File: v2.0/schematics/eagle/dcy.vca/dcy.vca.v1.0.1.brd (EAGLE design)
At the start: 100 x 50 mm, 104 parts, among them IC1 LM324N, IC2 4001N, IC3 TL074P, IC4 4001N, IC5 LM324N, IC6 TL074P

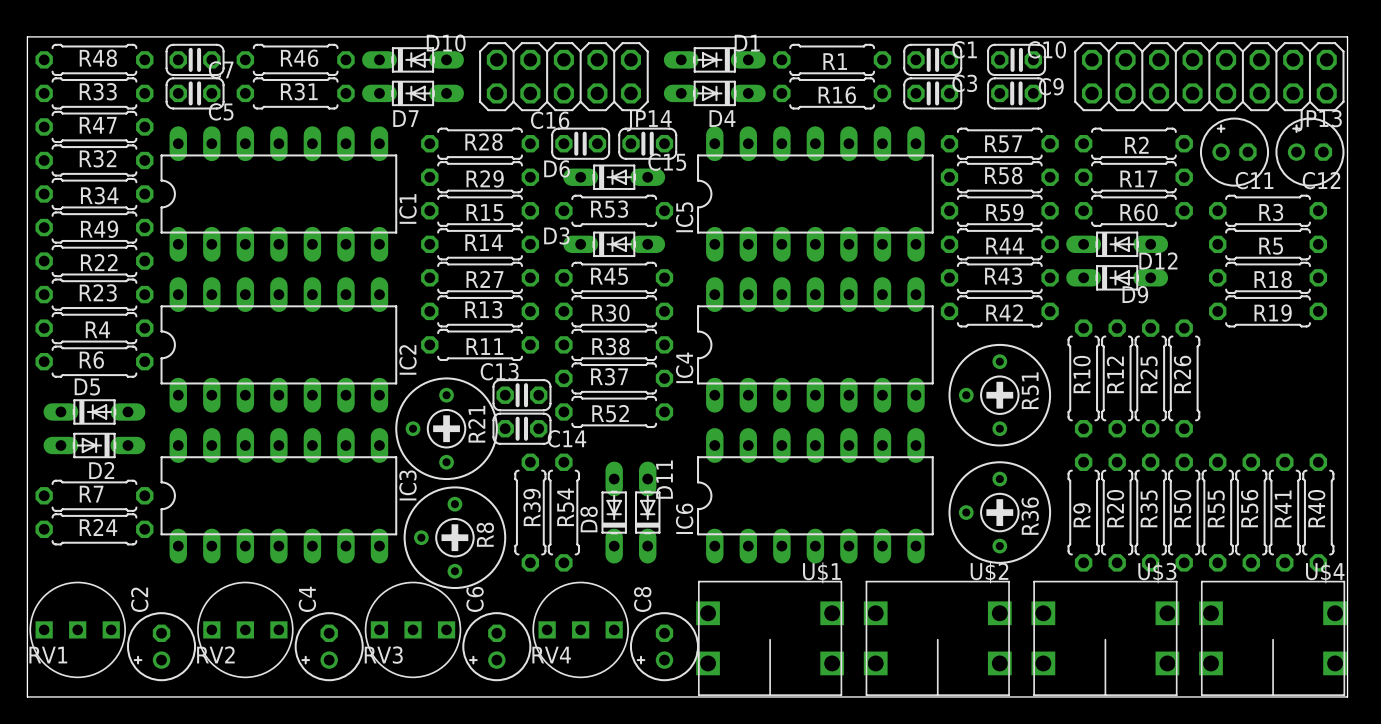
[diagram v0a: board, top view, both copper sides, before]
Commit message: Added panel board for quad decay and routed main and pnl
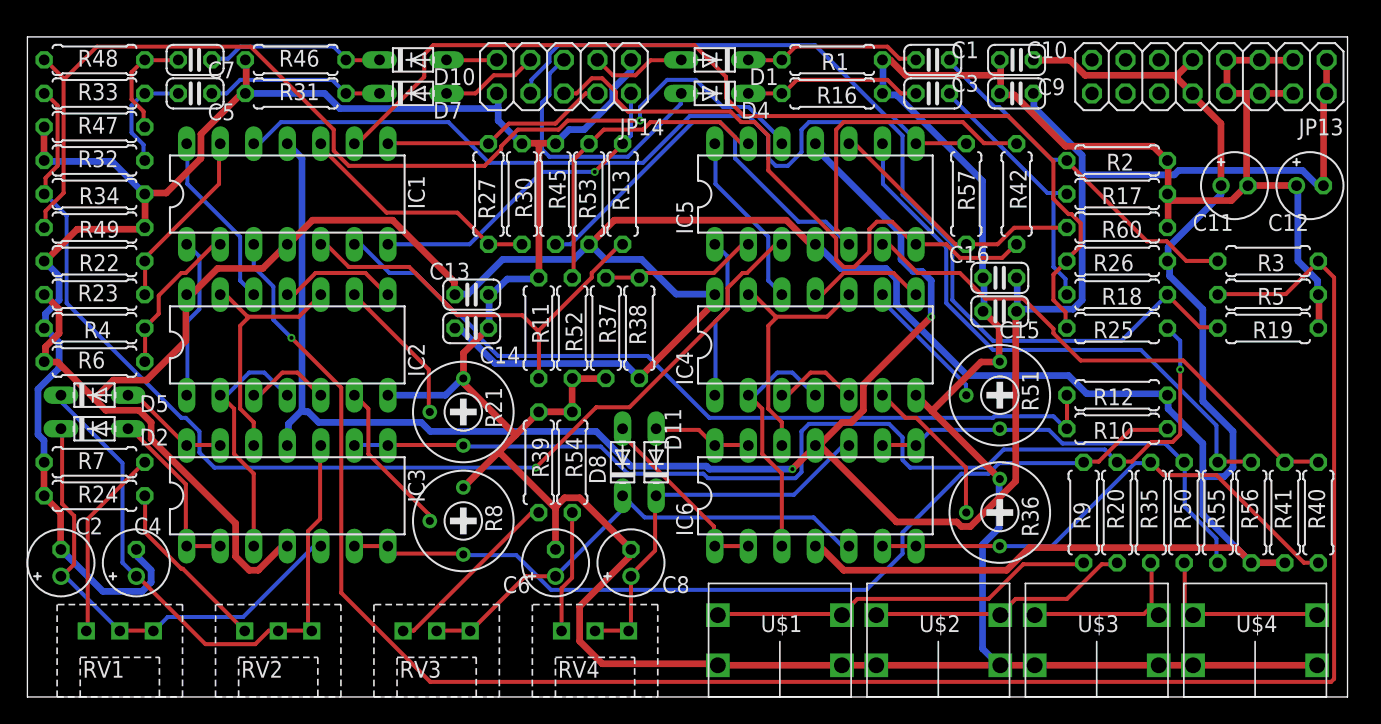
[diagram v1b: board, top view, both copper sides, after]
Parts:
- removed D12, D3, D6, D9: 1N5232B, _common:DO34-5
- removed R14, R28, R43, R58: 2.2K, _common:0207/7
- removed R15, R29, R44, R59: 1K, _common:0207/7
- moved C16 33.3 mm to (73.7, 31.8)
- moved C15 29.5 mm to (73.7, 29.2)
- moved C4 15.9 mm to (8.26, 10.2)
- moved R13 14.0 mm to (45.1, 38.1), turned to 90 degrees
- moved R18 11.5 mm to (82.5, 30.5)
- moved R30 11.3 mm to (37.5, 38.1), turned to 270 degrees
- moved R26 10.2 mm to (82.5, 33.0), turned to 180 degrees
- moved C2 9.92 mm to (2.54, 10.2)
- moved R42 8.98 mm to (74.9, 38.1), turned to 270 degrees
- moved C13 8.52 mm to (33.7, 30.5)
- moved C14 8.52 mm to (33.7, 27.9)
- moved R45 7.75 mm to (40.0, 38.1), turned to 270 degrees
- moved C6 7.75 mm to (40.0, 10.2)
- moved R52 7.10 mm to (41.3, 27.9), turned to 270 degrees
- moved C8 6.84 mm to (45.7, 10.2)
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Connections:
- removed net N$35: IC1.8, R27.2, R28.1
- removed net N$36: D6.C, R28.2, R29.1
- removed net N$5: IC1.7, R13.2, R14.1
- removed net N$54: IC5.7, R42.2, R43.1
- removed net N$55: D9.C, R43.2, R44.1
- removed net N$6: D3.C, R14.2, R15.1
- removed net N$74: IC5.8, R57.2, R58.1
- removed net N$75: D12.C, R58.2, R59.1
- net 0V: no longer D12.A, D3.A, D6.A, D9.A
- net N$EOC1: now also IC1.7, R13.2; no longer R15.2
- net N$EOC2: now also IC1.8, R27.2; no longer R29.2
- net N$EOC3: now also IC5.7, R42.2; no longer R44.2
- net N$EOC4: now also IC5.8, R57.2; no longer R59.2
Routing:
- net 0V: track 0.00 -> 372.8 mm
- net +12V: track 0.00 -> 273.3 mm
- net -12V: track 0.00 -> 182.0 mm, vias 0 -> 2
- net N$20: track 0.00 -> 148.1 mm, vias 0 -> 1
- net N$13: track 0.00 -> 95.9 mm
- net N$43: track 0.00 -> 85.8 mm, vias 0 -> 1
- net N$28: track 0.00 -> 79.9 mm, vias 0 -> 1
- net N$62: track 0.00 -> 79.6 mm, vias 0 -> 1
- net N$33: track 0.00 -> 76.5 mm
- net N$23: track 0.00 -> 69.0 mm
- net N$2: track 0.00 -> 62.5 mm
- net N$53: track 0.00 -> 54.5 mm
- net N$EOC3: track 0.00 -> 47.5 mm
- net N$31: track 0.00 -> 46.6 mm
- net N$72: track 0.00 -> 43.8 mm
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
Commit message: Flipped oritentaiton of panel board Changed power header to 2x5 hearder
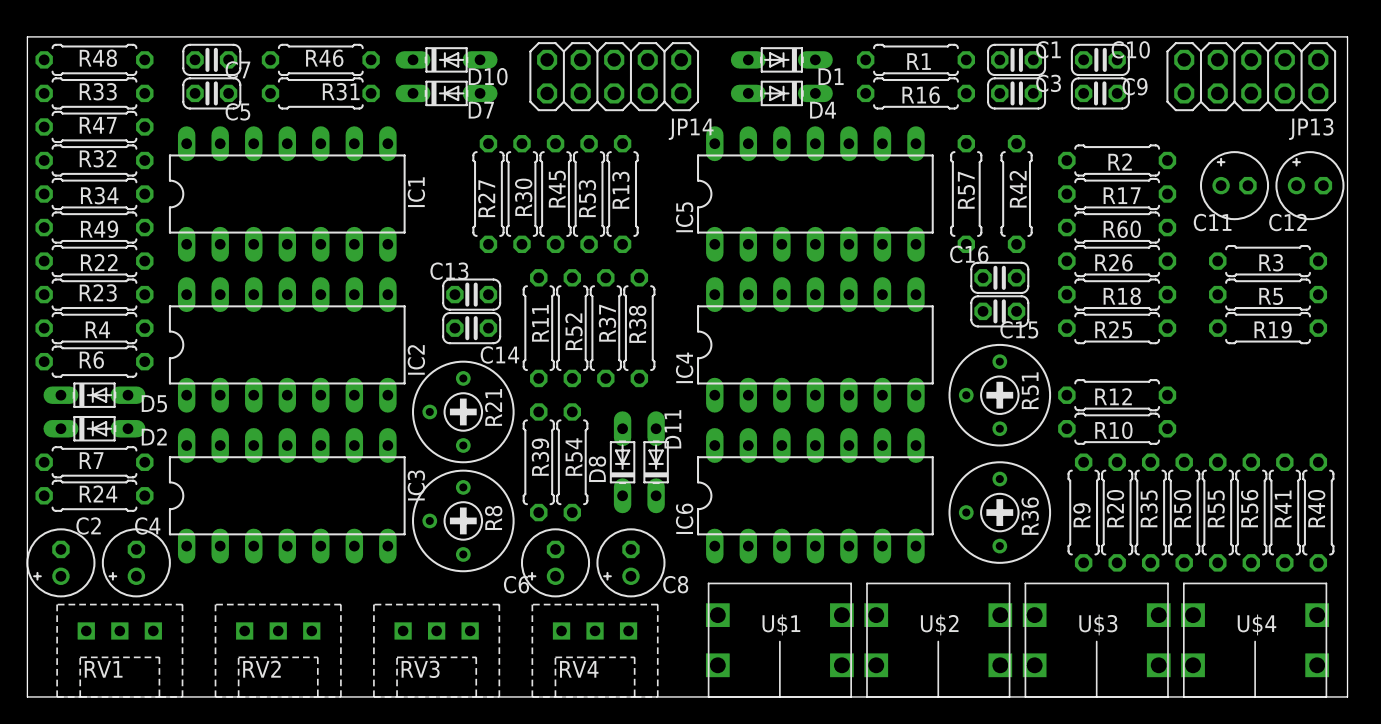
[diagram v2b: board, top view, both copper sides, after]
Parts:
- JP13: device pinhead:2X08 -> pinhead:2X05
- moved C1 6.35 mm to (74.9, 48.3)
- moved C3 6.35 mm to (74.9, 45.7)
- moved R1 6.35 mm to (67.3, 48.3)
- moved R16 6.35 mm to (67.3, 45.7)
- moved C10 6.35 mm to (81.3, 48.3)
- moved C9 6.35 mm to (81.3, 45.7)
- moved D1 5.08 mm to (57.1, 48.3)
- moved D4 5.08 mm to (57.1, 45.7)
- moved JP14 3.81 mm to (44.5, 47.0)
- moved JP13 3.17 mm to (92.7, 47.0)
- moved D10 2.54 mm to (31.8, 48.3)
- moved D7 2.54 mm to (31.8, 45.7)
- moved R31 1.91 mm to (22.2, 45.7)
- moved R46 1.91 mm to (22.2, 48.3)
- moved C5 1.27 mm to (14.0, 45.7)
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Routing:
- net 0V: track 372.8 -> 0.00 mm
- net +12V: track 273.3 -> 0.00 mm
- net -12V: track 182.0 -> 0.00 mm, vias 2 -> 0
- net N$20: track 148.1 -> 0.00 mm, vias 1 -> 0
- net N$13: track 95.9 -> 0.00 mm
- net N$43: track 85.8 -> 0.00 mm, vias 1 -> 0
- net N$28: track 79.9 -> 0.00 mm, vias 1 -> 0
- net N$62: track 79.6 -> 0.00 mm, vias 1 -> 0
- net N$33: track 76.5 -> 0.00 mm
- net N$23: track 69.0 -> 0.00 mm
- net N$2: track 62.5 -> 0.00 mm
- net N$53: track 54.5 -> 0.00 mm
- net N$EOC3: track 47.5 -> 0.00 mm
- net N$31: track 46.6 -> 0.00 mm
- net N$72: track 43.8 -> 0.00 mm
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
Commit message: Updated routing and jack position.
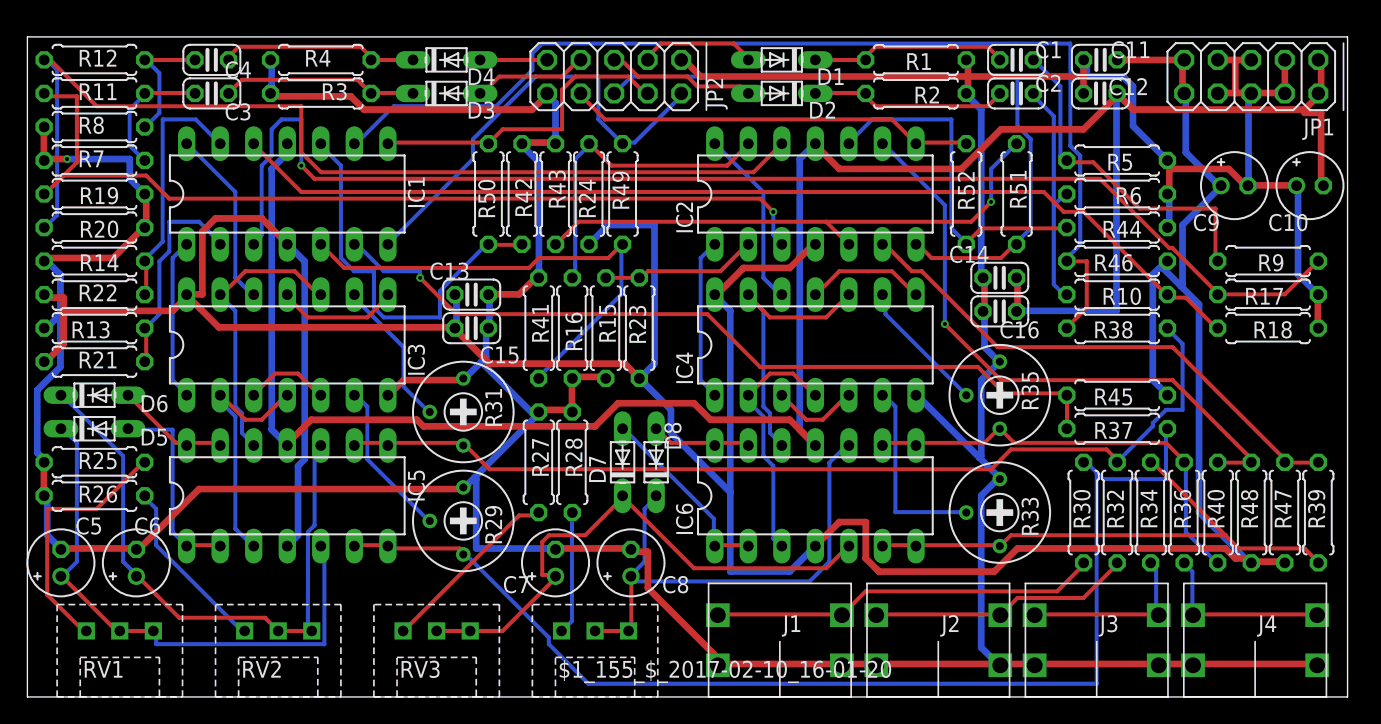
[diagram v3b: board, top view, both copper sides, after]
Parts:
- removed D10, D11: 1N4148, _common:DO34-5
- removed R53, R57: 3.3M, _common:0207/7
- removed R55: 330K, _common:0207/7
- removed R56: 10M, _common:0207/7
- added D3, D6: 1N4148, _common:DO34-5
- added R14, R15: 470, _common:0207/7
- added R29: 100K, rcl:RTRIM3339P
- added R43: 3.3M, _common:0207/7
- C10, C9: value 0.1uF -> 10uF; device _common:C025-024X044 -> _common:E2-5
- C11, C12: value 10uF -> 0.1uF; device _common:E2-5 -> _common:C025-024X044
- C2, C4: value 10uF -> 10n; device _common:E2-5 -> _common:C025-024X044
- C5, C7: value 10n -> 10uF; device _common:C025-024X044 -> _common:E2-5
- IC2: value 4001N -> LM324N; device 40xx:DIL14 -> linear:DIL14
- IC3: value TL074P -> 4001N; device _common:DIL14 -> 40xx:DIL14
- IC5: value LM324N -> TL074P; device linear:DIL14 -> _common:DIL14
- R10: value 330K -> 47K
- R11, R6: value 3.3M -> 47K
- R12: value 10M -> 47K
- R13: value 3.3M -> 470
- R16: value 100K -> 470
- R17, R18, R2, R3: value 47K -> 100K
- R20: value 1K -> 100K
- R21, R51: value 100K -> 3.3M; device rcl:RTRIM3339P -> _common:0207/7
- R22, R52: value 470 -> 3.3M
- R24: value 2.2K -> 3.3M
- R25: value 330K -> 2.2K
- R26: value 10M -> 2.2K
- R27: value 3.3M -> 2.2K
- R30: value 3.3M -> 1K
- R31: device _common:0207/7 -> rcl:RTRIM3339P
- R32: value 47K -> 1K
- R33: value 47K -> 100K; device _common:0207/7 -> rcl:RTRIM3339P
- R34: value 100K -> 1K
- R35: value 1K -> 100K; device _common:0207/7 -> rcl:RTRIM3339P
- R36: value 100K -> 1K; device rcl:RTRIM3339P -> _common:0207/7
- R37: value 470 -> 330K
- R38: value 3.3M -> 330K
- R39: value 2.2K -> 330K
- R4: value 470 -> 100K
- R41: value 10M -> 3.3M
- R45: value 3.3M -> 10M
- R46: value 100K -> 10M
- R47, R48: value 47K -> 10M
- R49: value 100K -> 3.3M
- R5: value 100K -> 47K
- R50: value 1K -> 3.3M
- R7: value 2.2K -> 47K
- R8: value 100K -> 47K; device rcl:RTRIM3339P -> _common:0207/7
- R9: value 1K -> 47K
- moved R47 94.8 mm to (95.2, 14.0), turned to 90 degrees
- moved R48 94.1 mm to (92.7, 14.0), turned to 90 degrees
- moved R19 89.5 mm to (5.08, 38.1)
- moved R34 83.6 mm to (85.1, 14.0), turned to 90 degrees
- moved R32 81.9 mm to (82.5, 14.0), turned to 90 degrees
- moved R12 81.5 mm to (5.08, 48.3), turned to 0 degrees
- moved C2 80.7 mm to (74.9, 45.7), turned to 0 degrees
- moved R20 80.4 mm to (5.08, 35.6), turned to 180 degrees
- moved R26 79.5 mm to (5.08, 15.2), turned to 0 degrees
- moved R6 78.5 mm to (82.5, 38.1), turned to 180 degrees
- moved R25 78.1 mm to (5.08, 17.8), turned to 0 degrees
- moved R33 75.6 mm to (73.7, 14.0), turned to 270 degrees
- moved R3 72.9 mm to (22.2, 45.7), turned to 0 degrees
- moved R46 62.2 mm to (82.5, 33.0), turned to 180 degrees
- moved C3 61.0 mm to (14.0, 45.7), turned to 180 degrees
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- renumbered JP13 to JP1, JP14 to JP2, R54 to R28, R60 to R44, RV4 to $1_155_$_2017-02-10_16-01-20, U$1 to J1, U$2 to J2, U$3 to J3, U$4 to J4
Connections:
- net +12V: now also C11.2, C15.2, C9.+, IC2.4, IC3.14, R21.1, R22.1, R24.1, R45.1, R46.1, R47.1, R48.1; no longer C10.2, C11.+, C14.2, IC2.14, IC3.4, R12.1, R26.1, R38.1, R41.1, R53.1, R56.1, R6.1
- net -12V: now also C10.-, C12.1, C14.1, IC2.11; no longer C12.-, C15.1, C9.1, IC3.11
- net 0V: now also C10.+, C11.1, C12.2, C14.2, C15.1, C5.-, C7.-, C9.-, IC3.7, R13.2, R14.2, R15.2, R16.2, R18.1, R20.1, R25.1, R26.1, R27.1, R29.1, R3.1, R33.1, R35.1, R4.1, R41.1, R42.1, R43.1, R6.1; no longer C10.1, C11.-, C12.+, C14.1, C15.2, C2.-, C4.-, C9.2, IC2.7, R11.1, R16.1, R21.1, R22.2, R24.1, R30.1, R32.1, R34.1, R36.1, R37.2, R39.1, R4.2, R45.1, R46.1, R47.1, R49.1, R51.1, R52.2
- net N$1: now also R25.2; no longer R7.2
- net N$11: now also C2.1, D2.C, R2.2; no longer C3.1, D4.C, R16.2
- net N$12: now also C2.2, R10.2, R6.2; no longer C3.2, R17.2, R18.2
- net N$13: now also R10.1, R18.2; no longer R18.1, R19.2
- net N$14: now also IC3.2, IC3.4, IC5.3; no longer IC2.2, IC2.4, IC3.3
- net N$16: now also R14.1, R22.2; no longer R22.1, R23.2
- net N$17: now also D5.A, IC5.1, IC5.2; no longer D2.A, IC3.1, IC3.2
- net N$19: now also R5.2, R9.2; no longer R2.2, R3.2
- net N$2: now also R37.2, R45.2; no longer R10.2, R12.2
- net N$20: now also R17.2, R9.1; no longer R3.1, R5.2
- net N$21: now also R13.1, R21.2; no longer R4.1, R6.2
- net N$22: now also IC3.1; no longer IC2.1
- net N$23: now also IC5.6, IC5.7, R29.3, R30.2, R37.1; no longer IC3.6, IC3.7, R10.1, R8.3, R9.2
- net N$24: now also R30.1; no longer R9.1
- net N$25: now also IC3.6, R29.2; no longer IC2.6, R8.2
- net N$26: now also IC3.12; no longer IC2.12
- net N$27: now also D6.A, IC5.13, IC5.14; no longer D5.A, IC3.13, IC3.14
- net N$28: now also IC5.8, IC5.9, R31.3, R32.2, R38.1; no longer IC3.8, IC3.9, R20.2, R21.3, R25.1
- net N$29: now also R32.1; no longer R20.1
- net N$3: now also R41.2, R49.1; no longer R11.2, R13.1
- net N$30: now also IC3.9, R31.2; no longer IC2.9, R21.2
- net N$31: now also C6.+, D6.C, IC5.10; no longer C4.+, D5.C, IC3.10
- net N$32: now also R26.2; no longer R24.2
- net N$33: now also R38.2, R46.2; no longer R25.2, R26.2
- net N$34: now also R42.2, R50.1; no longer R27.1, R30.2
- net N$4: now also IC3.3, IC3.5; no longer IC2.3, IC2.5
- net N$41: now also C3.1, D3.C, R3.2; no longer C5.1, D7.C, R31.2
- net N$42: now also C3.2, R11.2, R7.2; no longer C5.2, R32.2, R33.2
- net N$43: now also IC2.3, R11.1, R19.2; no longer IC5.3, R33.1, R34.2
- net N$44: now also IC2.2, R15.1, R23.2; no longer IC5.2, R37.1, R38.2
- net N$45: now also IC2.1; no longer IC5.1
- net N$46: now also D7.A; no longer D8.A
- net N$47: now also R33.3, R34.2, R39.1; no longer R35.2, R36.3, R40.1
- net N$48: now also R34.1; no longer R35.1
- net N$49: now also R33.2; no longer R36.2
- net N$50: now also C7.+, D7.C; no longer C6.+, D8.C
- net N$51: now also R27.2; no longer R39.2
- net N$52: now also IC2.6, R39.2, R47.2; no longer IC5.6, R40.2, R41.2
- net N$53: now also IC2.5, R43.2, R51.1; no longer IC5.5, R42.1, R45.2
- net N$60: now also C4.1, D4.C, R4.2; no longer C7.1, D10.C, R46.2
- net N$61: now also C4.2, R12.2, R8.2; no longer C7.2, R47.2, R48.2
- net N$62: now also IC2.12, R12.1, R20.2; no longer IC5.12, R48.1, R49.2
- net N$63: now also C5.+, D5.C, IC5.5; no longer C2.+, D2.C, IC3.5
- net N$64: now also IC2.13, R16.1, R24.2; no longer IC5.13, R52.1, R53.2
- net N$65: now also IC2.14; no longer IC5.14
- net N$66: now also D8.A; no longer D11.A
- net N$67: now also R35.3, R36.2, R40.1; no longer R50.2, R51.3, R55.1
- net N$68: now also R36.1; no longer R50.1
- net N$69: now also R35.2; no longer R51.2
- net N$70: now also D8.C; no longer D11.C
- net N$72: now also IC2.9, R40.2, R48.2; no longer IC5.9, R55.2, R56.2
- net N$73: now also IC2.10, R52.1; no longer IC5.10, R57.1
- net N$8: now also IC3.11, IC3.8; no longer IC2.11, IC2.8
- net N$9: now also IC3.10, IC3.13, IC5.12; no longer IC2.10, IC2.13, IC3.12
- net N$EOC1: now also R49.2; no longer R13.2
- net N$EOC2: now also R50.2; no longer R27.2
- net N$EOC3: now also IC2.7, R51.2; no longer IC5.7, R42.2
- net N$EOC4: now also IC2.8, R52.2; no longer IC5.8, R57.2
- net N$TRG2: now also D2.A; no longer D4.A
- net N$TRG3: now also D3.A; no longer D7.A
- net N$TRG4: now also D4.A; no longer D10.A
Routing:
- net 0V: track 0.00 -> 388.2 mm, vias 0 -> 1
- net +12V: track 0.00 -> 263.7 mm
- net -12V: track 0.00 -> 170.1 mm
- net N$20: track 0.00 -> 97.5 mm, vias 0 -> 1
- net N$23: track 0.00 -> 87.6 mm
- net N$33: track 0.00 -> 82.5 mm
- net N$13: track 0.00 -> 78.8 mm
- net N$62: track 0.00 -> 76.0 mm
- net N$28: track 0.00 -> 73.5 mm
- net N$43: track 0.00 -> 68.6 mm, vias 0 -> 1
- net N$2: track 0.00 -> 61.5 mm, vias 0 -> 1
- net N$EOC3: track 0.00 -> 53.1 mm
- net N$72: track 0.00 -> 45.9 mm, vias 0 -> 1
- net N$31: track 0.00 -> 45.8 mm
- net N$63: track 0.00 -> 42.5 mm
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
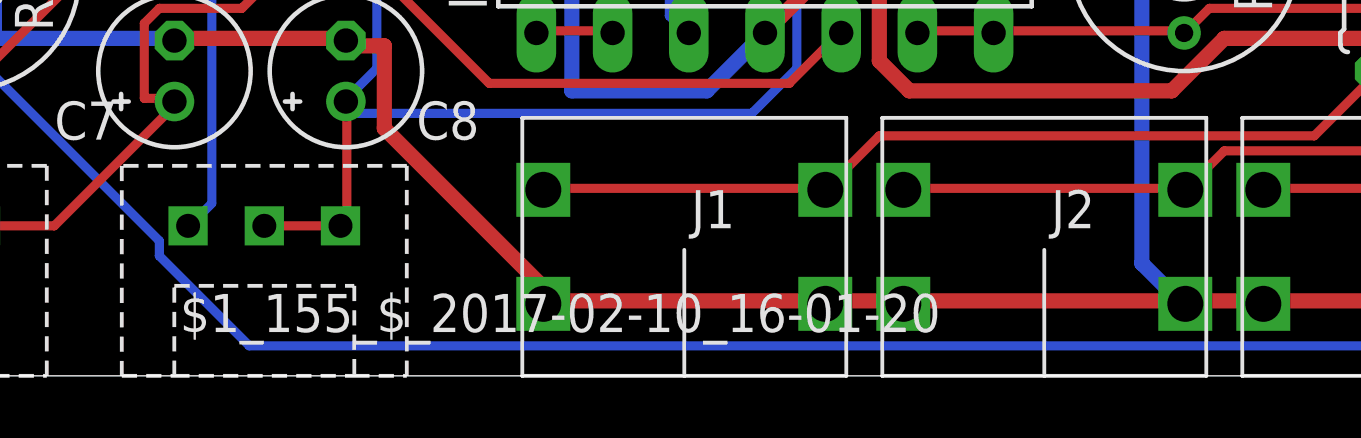
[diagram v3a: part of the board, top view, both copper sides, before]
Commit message: Generated gerber files for quad decay boards for Seeed order
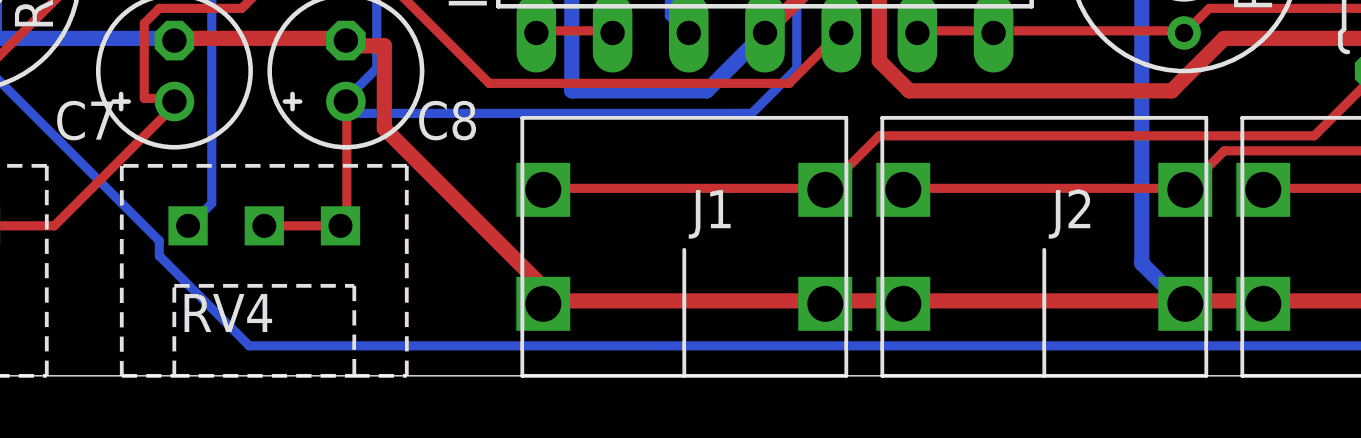
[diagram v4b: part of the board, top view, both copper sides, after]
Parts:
- renumbered $1_155_$_2017-02-10_16-01-20 to RV4
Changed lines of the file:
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@@
 <element name="RV2" library="_common" package="R-VAR" value="50K (A)" x="19" y="5" locked="yes"/>
 <element name="RV3" library="_common" package="R-VAR" value="50K (A)" x="31" y="5" locked="yes"/>
-<element name="$1_155_$_2017-02-10_16-01-20" library="_common" package="R-VAR" value="50K (A)" x="43" y="5" locked="yes"/>
+<element name="RV4" library="_common" package="R-VAR" value="50K (A)" x="43" y="5" locked="yes"/>
 <element name="J1" library="jacks" package="CL1384" value="OUT1" x="61.7" y="2.4" locked="yes" smashed="yes" rot="R180">
 <attribute name="NAME" x="58.69" y="6.19" size="1.27" layer="25" rot="R180"/>
@@
 <signal name="N$70">
 <contactref element="IC6" pad="10"/>
-<contactref element="$1_155_$_2017-02-10_16-01-20" pad="R2"/>
+<contactref element="RV4" pad="R2"/>
 <contactref element="D8" pad="C"/>
-<contactref element="$1_155_$_2017-02-10_16-01-20" pad="VAR"/>
+<contactref element="RV4" pad="VAR"/>
 <contactref element="C8" pad="+"/>
 <wire x1="45.54" y1="5" x2="43" y2="5" width="0.3048" layer="1"/>
@@
 </signal>
 <signal name="N$71">
-<contactref element="$1_155_$_2017-02-10_16-01-20" pad="R1"/>
+<contactref element="RV4" pad="R1"/>
 <contactref element="R28" pad="2"/>
 <wire x1="41.25" y1="5.75" x2="40.5" y2="5" width="0.3048" layer="16"/>
